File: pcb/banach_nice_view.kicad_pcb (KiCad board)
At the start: 2 copper layers, 132.3 x 90.7 mm, 68 parts, among them J1 MJ-4PP-9, J2 OLED, SW10 SW_PUSH, SW11 SW_PUSH, SW12 SW_PUSH, SW14 SW_PUSH, SW15 SW_PUSH, SW16 SW_PUSH, SW17 SW_PUSH, SW18 SW_PUSH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

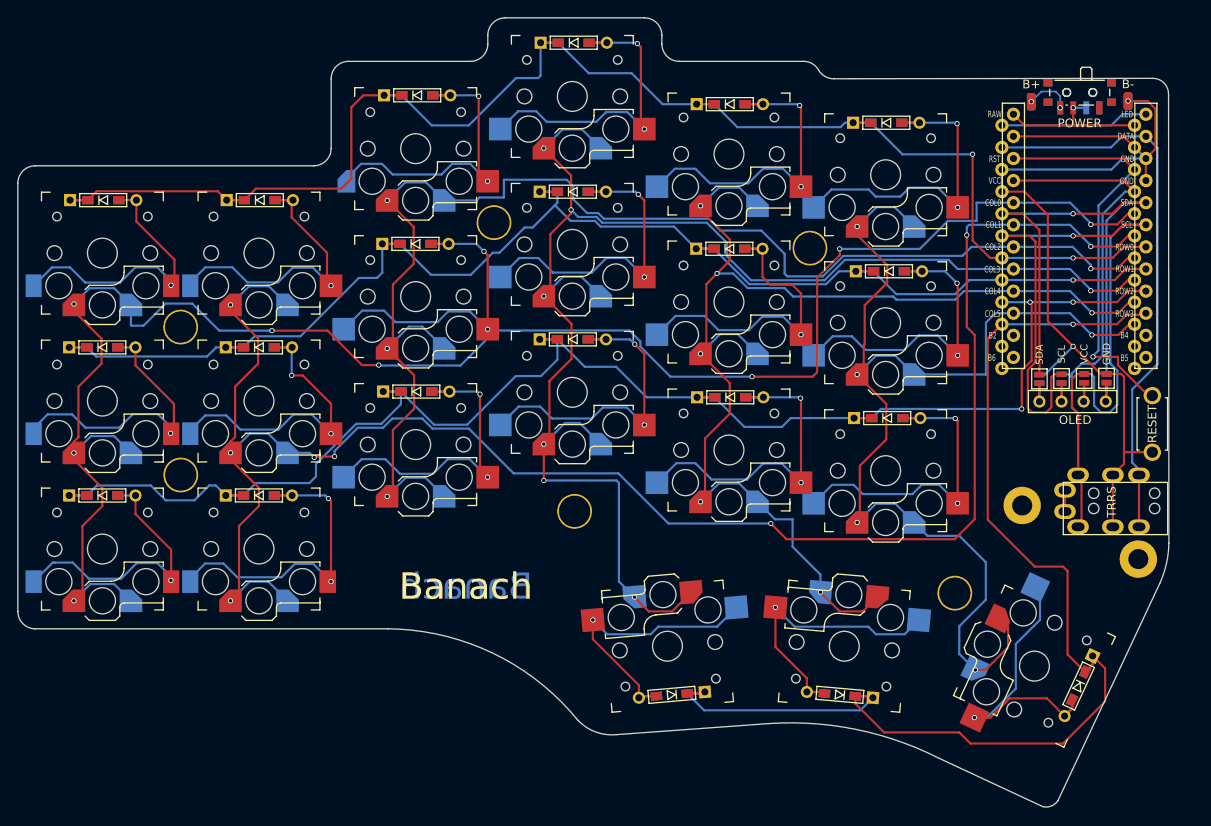
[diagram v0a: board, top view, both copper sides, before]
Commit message: Moved power switch to top of the board where the USB port will be located. Increased through hole diameter for screws and standoffs. Completed top and bottom plates. Attempting to make version for 5pin OLED.
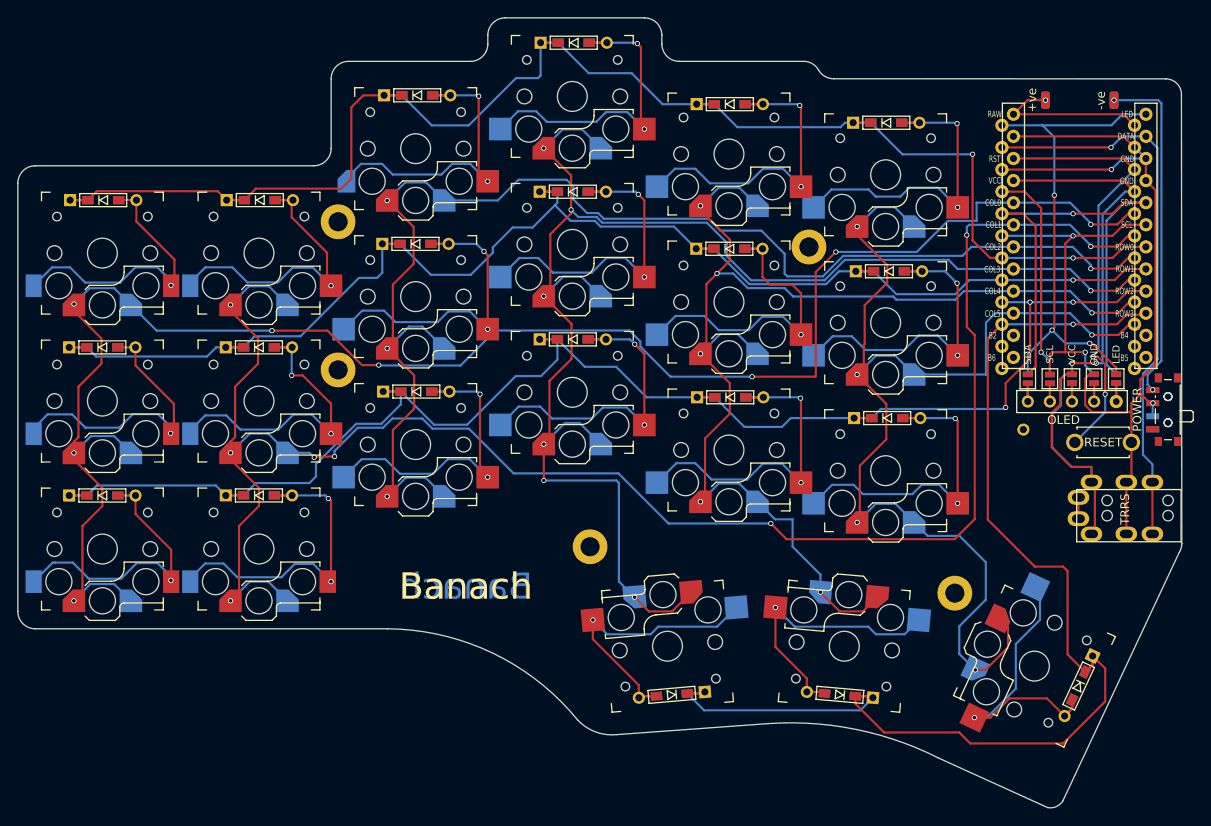
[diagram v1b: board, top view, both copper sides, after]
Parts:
- removed h1: h1, kbd:LEGO_HOLE
- removed h2: h2, kbd:LEGO_HOLE
- removed the h7 at (173.6, 99.4)
- removed h8: h8, kbd:LEGO_HOLE
- added ?: , , F.Cu at (173.7, 90.7)
- added JP62: GND, foostan:Jumper, B.Cu at (174.2, 84.8)
- added JP68: LED, foostan:Jumper, F.Cu at (184.4, 84.8)
- added h4: h4, kbd:LEGO_HOLE, F.Cu at (124.0, 104.1)
- +ve (x2): renamed from B+; value B+ -> SolderWirePad_1x01_SMD_1x2mm
- -ve (x2): renamed from B-; value B- -> SolderWirePad_1x01_SMD_1x2mm
- h3: renamed from h4; value h4 -> h3
- h5: renamed from h3; value h3 -> h5
- h7: renamed from h5; value h5 -> h7
- moved POWER 37.4 mm to (190.0, 88.4), turned to 90 degrees
- moved POWER 37.4 mm to (190.0, 88.4), turned to -90 degrees
- moved h5 31.7 mm to (95.0, 83.8)
- moved h6 17.9 mm to (95.0, 66.8)
- moved RSW1 6.03 mm to (182.9, 92.2), turned to 0 degrees
- moved J1 1.75 mm to (191.9, 100.6)
- moved +ve 1.65 mm to (176.3, 52.8) (x2)
- moved -ve 1.61 mm to (184.2, 52.8) (x2)
- moved JP68 1.43 mm to (181.9, 84.8)
- moved JP65 1.40 mm to (179.3, 84.8)
- moved JP63 1.34 mm to (176.8, 84.8)
- moved J2 1.34 mm to (174.2, 87.5)
- moved JP61 1.34 mm to (174.2, 84.8)
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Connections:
- +ve pad 1: Batt+ -> Net-(U1-Pad24) (x2)
- JP6 pad 2: Net-(U1-Pad12) -> NET-(U1-Pad10)
- JP62 pad 2: Net-(U1-Pad14) -> Net-(U1-Pad13)
- JP64 pad 2: Net-(U1-Pad13) -> Net-(U1-Pad11)
- JP66 pad 2: Net-(U1-Pad11) -> Net-(U1-Pad12)
- POWER pad 2: RAW -> GND (x2)
- POWER pad 3: Batt+ -> GND
- POWER pad 1: Batt+ -> GND
- U1 pad 24: RAW -> Net-(U1-Pad24)
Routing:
- net GND: track 104.3 -> 158.4 mm, vias 2 -> 5
- net SCL: track 80.8 -> 40.2 mm, vias 1 -> 2
- net LED: track 17.1 -> 57.4 mm, vias 0 -> 3
- net Net-(U1-Pad24): track 0.00 -> 18.8 mm, vias 0 -> 1
- net RAW: track 18.0 -> 0.00 mm, vias 1 -> 0
- net VCC: track 72.4 -> 82.8 mm, vias 0 -> 2
- net Batt+: track 5.37 -> 0.00 mm, vias 2 -> 0
- net NET-(U1-Pad10): track 0.00 -> 4.25 mm
- net col0: track 207.2 -> 203.9 mm
- net reset: track 47.4 -> 50.3 mm, vias 1 -> 2
- net row2: track 176.6 -> 173.9 mm
- net col2: track 155.7 -> 154.5 mm
- net SDA: track 61.7 -> 62.4 mm
- net data: track 64.0 -> 64.5 mm, vias 0 -> 1
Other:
- board size 132.3 x 90.7 mm -> 133.7 x 90.8 mm
